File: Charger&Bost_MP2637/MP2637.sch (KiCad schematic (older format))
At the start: 45 parts

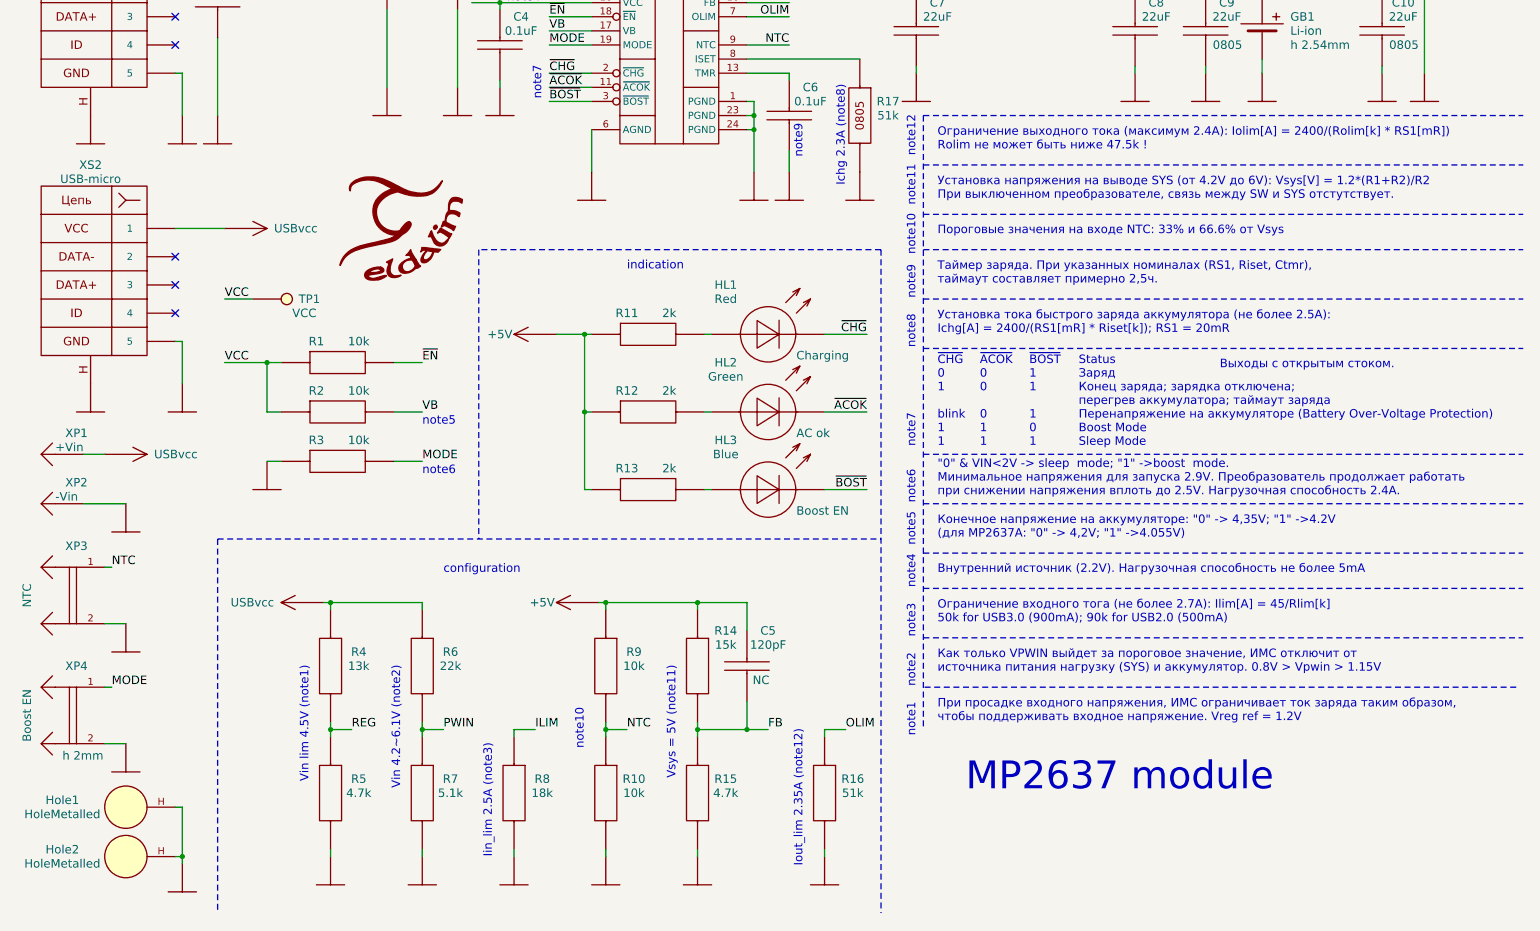
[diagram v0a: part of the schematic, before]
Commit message: MP2637: Трассировка завершена
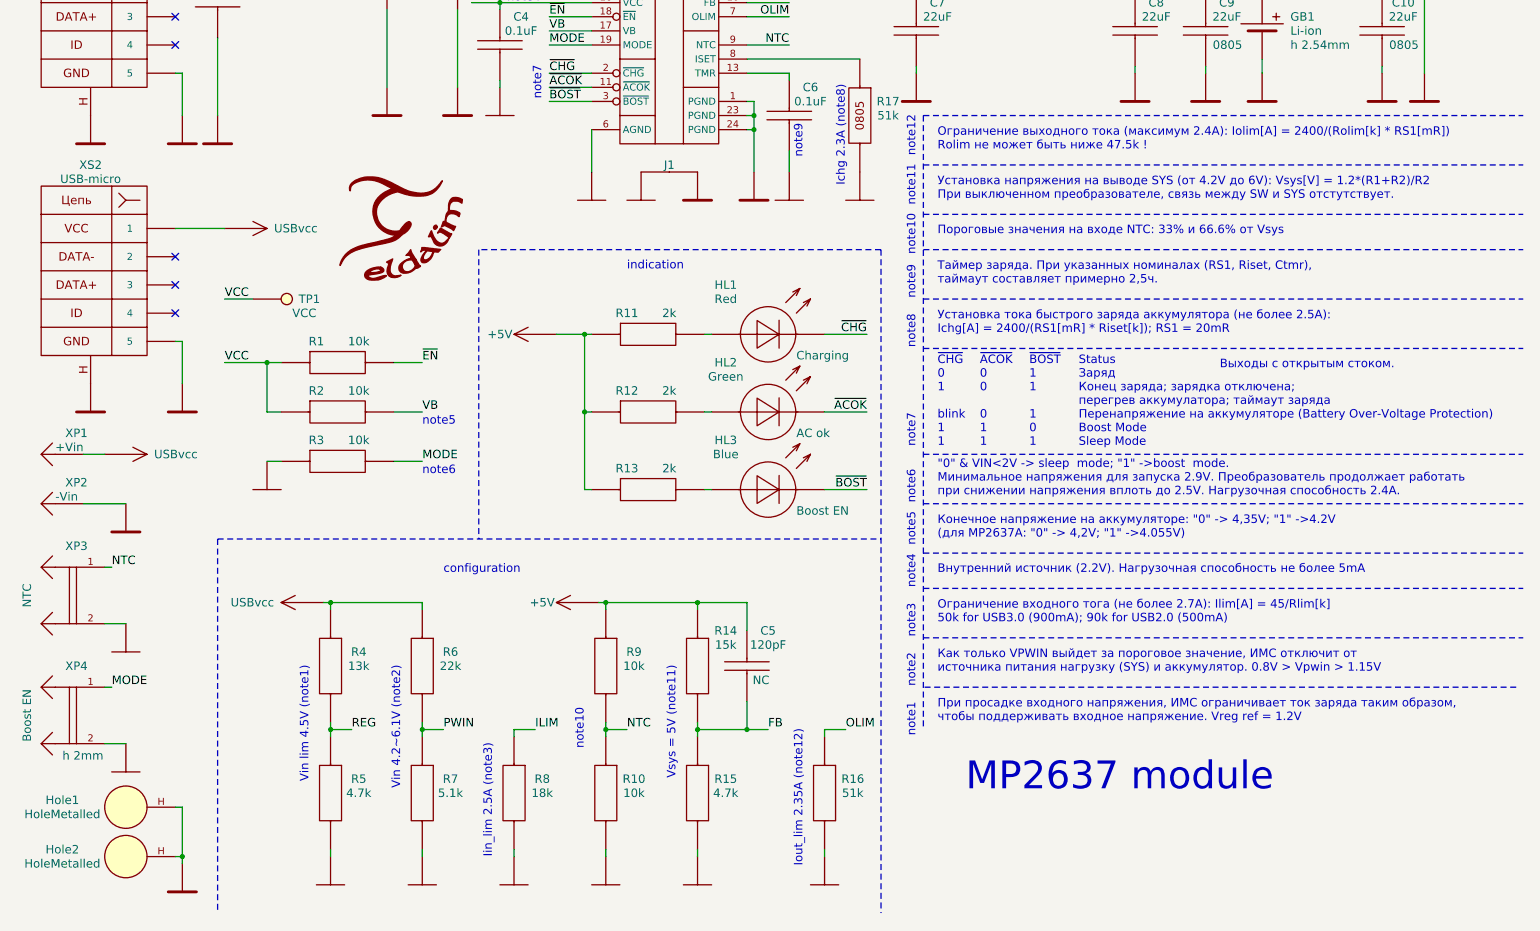
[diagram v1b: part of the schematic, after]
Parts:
- added J1: Jumper, symbol Jumper
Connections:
- net GND: now also J1.1, J1.2
